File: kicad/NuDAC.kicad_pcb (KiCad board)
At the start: 4 copper layers, 63.5 x 22.9 mm, 62 parts, among them CN1 2SJ3080-000111F, J1 2137160001, J2 Conn_01x14, J3 Conn_01x14, SW1 PTS820, U1 TPS2065CDBVR-2, U2 MCP1812BT-033_OT, U3 M482ZGCAE, U4 MCP1812AT-018_OT, U5 NAU88L25YGB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

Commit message: Add silkscreen comment
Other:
- board text added: "DANCHOUZHOU June 4, 2021 V1.0 https://github.com/danchouzhou/NuDAC"

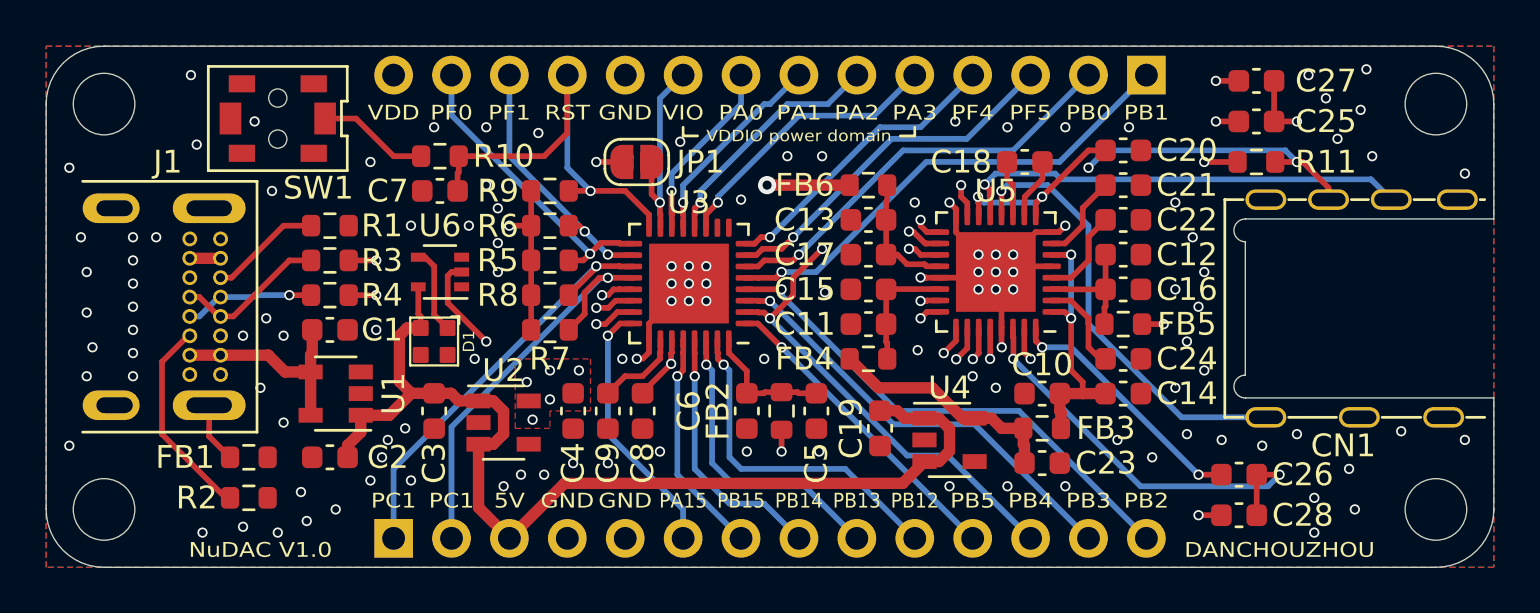
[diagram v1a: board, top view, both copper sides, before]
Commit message: Update to KiCad 6
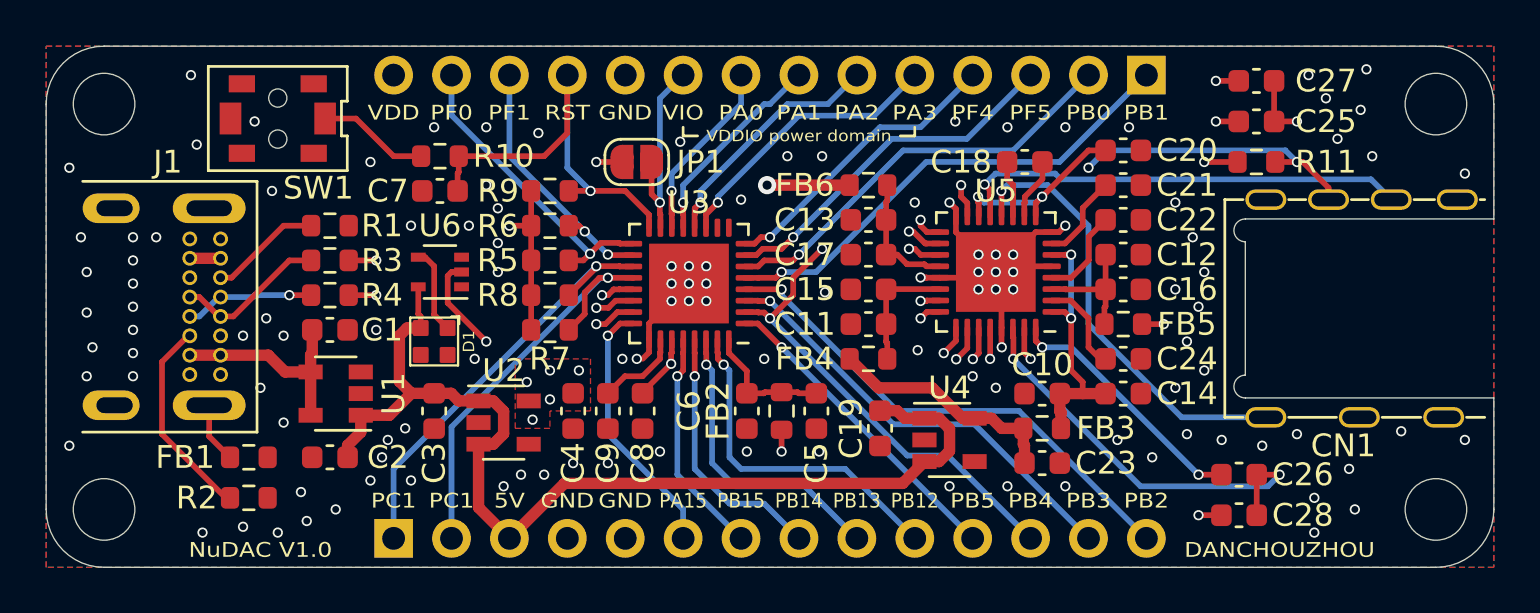
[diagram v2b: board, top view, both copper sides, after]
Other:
- net class Default removed
